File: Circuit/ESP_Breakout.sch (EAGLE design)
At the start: 15 parts, among them U1 AMS1117-3.3, X2 ESP-12

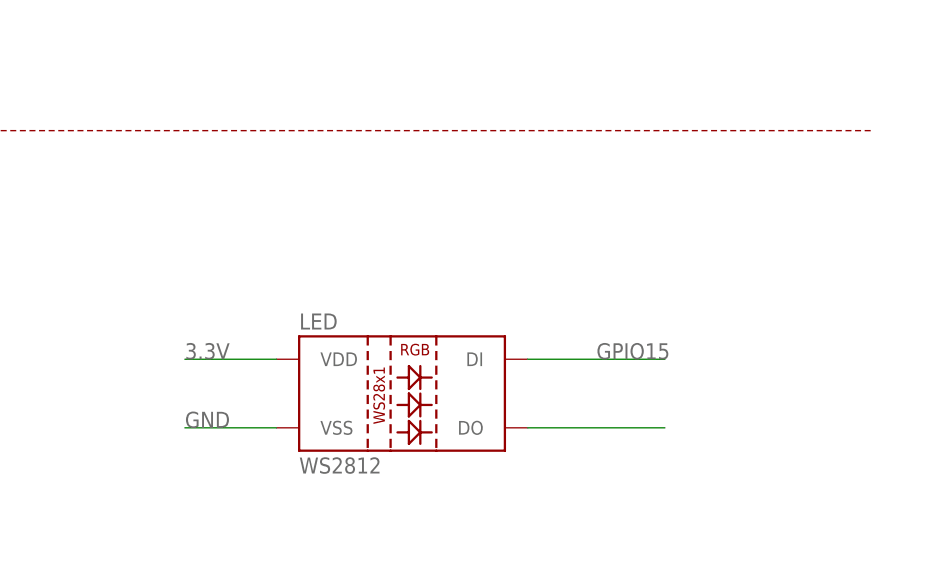
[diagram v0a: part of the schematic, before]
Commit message: car v3 with RGB, update platformio ESP dev structure
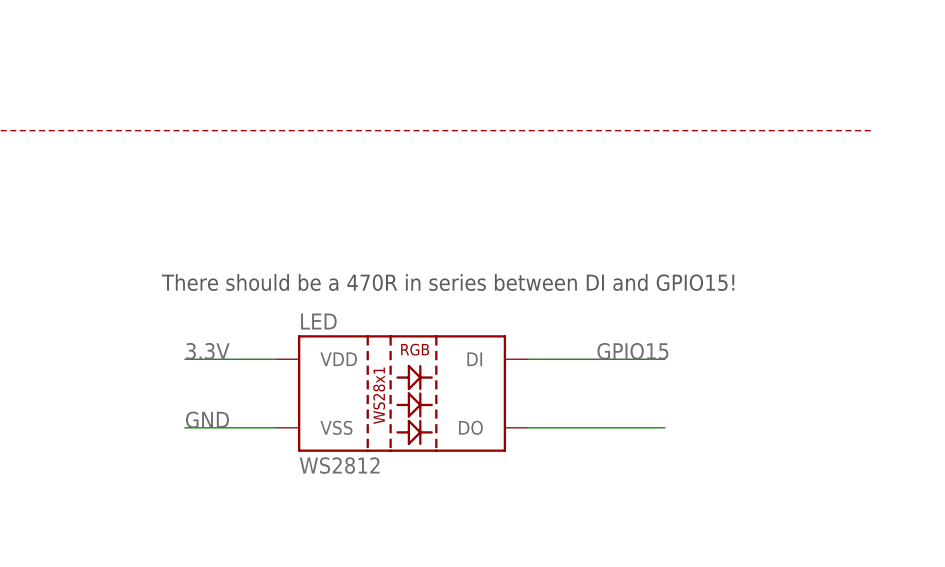
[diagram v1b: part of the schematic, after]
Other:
- note added: "There should be a 470R in series between DI and GPIO15!"
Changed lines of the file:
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@@
 <wire x1="256.54" y1="96.52" x2="142.24" y2="96.52" width="0.1524" layer="94" style="shortdash"/>
 <text x="40.64" y="116.84" size="1.778" layer="94">ESP8266 MODULE + AUTORESET</text>
+<text x="177.8" y="78.74" size="1.778" layer="97">There should be a 470R in series between DI and GPIO15!</text>
 </plain>
 <instances>
